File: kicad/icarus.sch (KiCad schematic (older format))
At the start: 80 parts, among them J1 CAN Bus, J2 CAN Bus, J3 SWD Programming, J4 USB_B_Micro, U1 MAX15062A, U10 XT30, U11 XT30, U12 XT30, U13 LT1787HVIMS8PBF, U14 USBLC6-2SC6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

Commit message: Updated BOM, updated layout to fix design rules
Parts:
- CR1, CR2: symbol SMBJ51CA-E3&slash_52:SMBJ51CA-E3_52 -> icarus-rescue:SMBJ51CA-E3_52-SMBJ51CA-E3&slash_52
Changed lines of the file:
@@
 	7200 3525 7475 3525
 $Comp
-L SMBJ51CA-E3&slash_52:SMBJ51CA-E3_52 CR1
+L icarus-rescue:SMBJ51CA-E3_52-SMBJ51CA-E3&slash_52 CR1
 U 1 1 608E4AFE
 P 7475 3925
@@
 Connection ~ 7475 3525
 $Comp
-L SMBJ51CA-E3&slash_52:SMBJ51CA-E3_52 CR2
+L icarus-rescue:SMBJ51CA-E3_52-SMBJ51CA-E3&slash_52 CR2
 U 1 1 608F0D36
 P 7675 3925

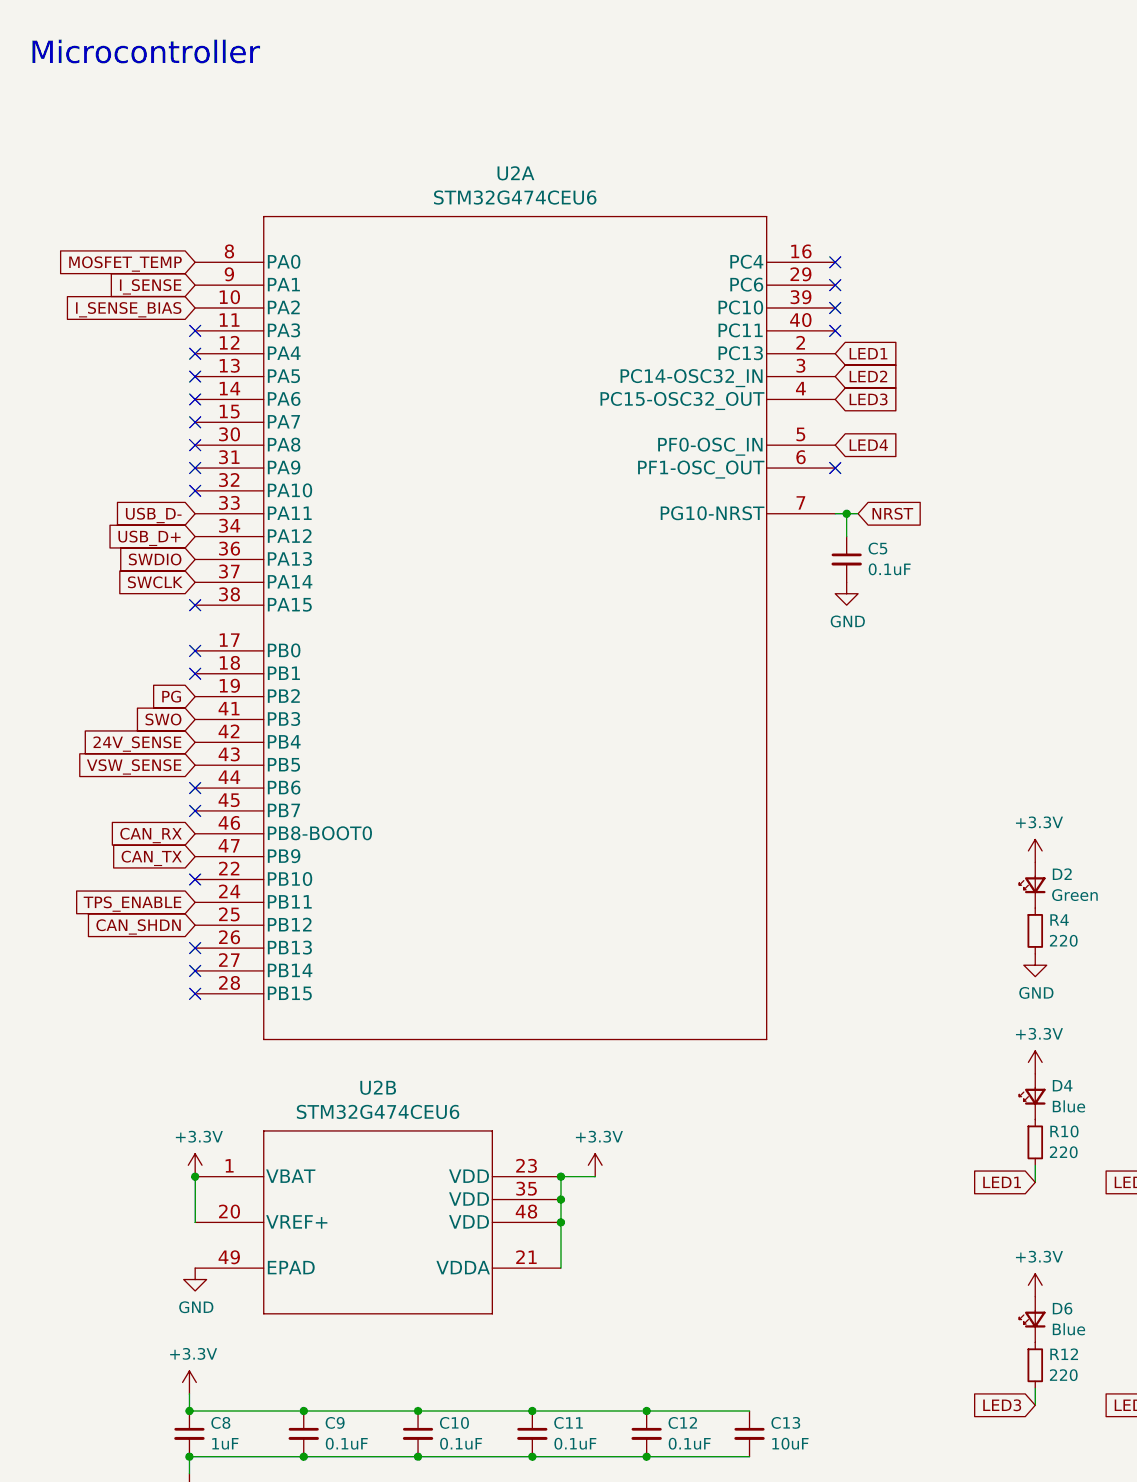
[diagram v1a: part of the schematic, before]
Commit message: Changed MCU due to sourcing problems
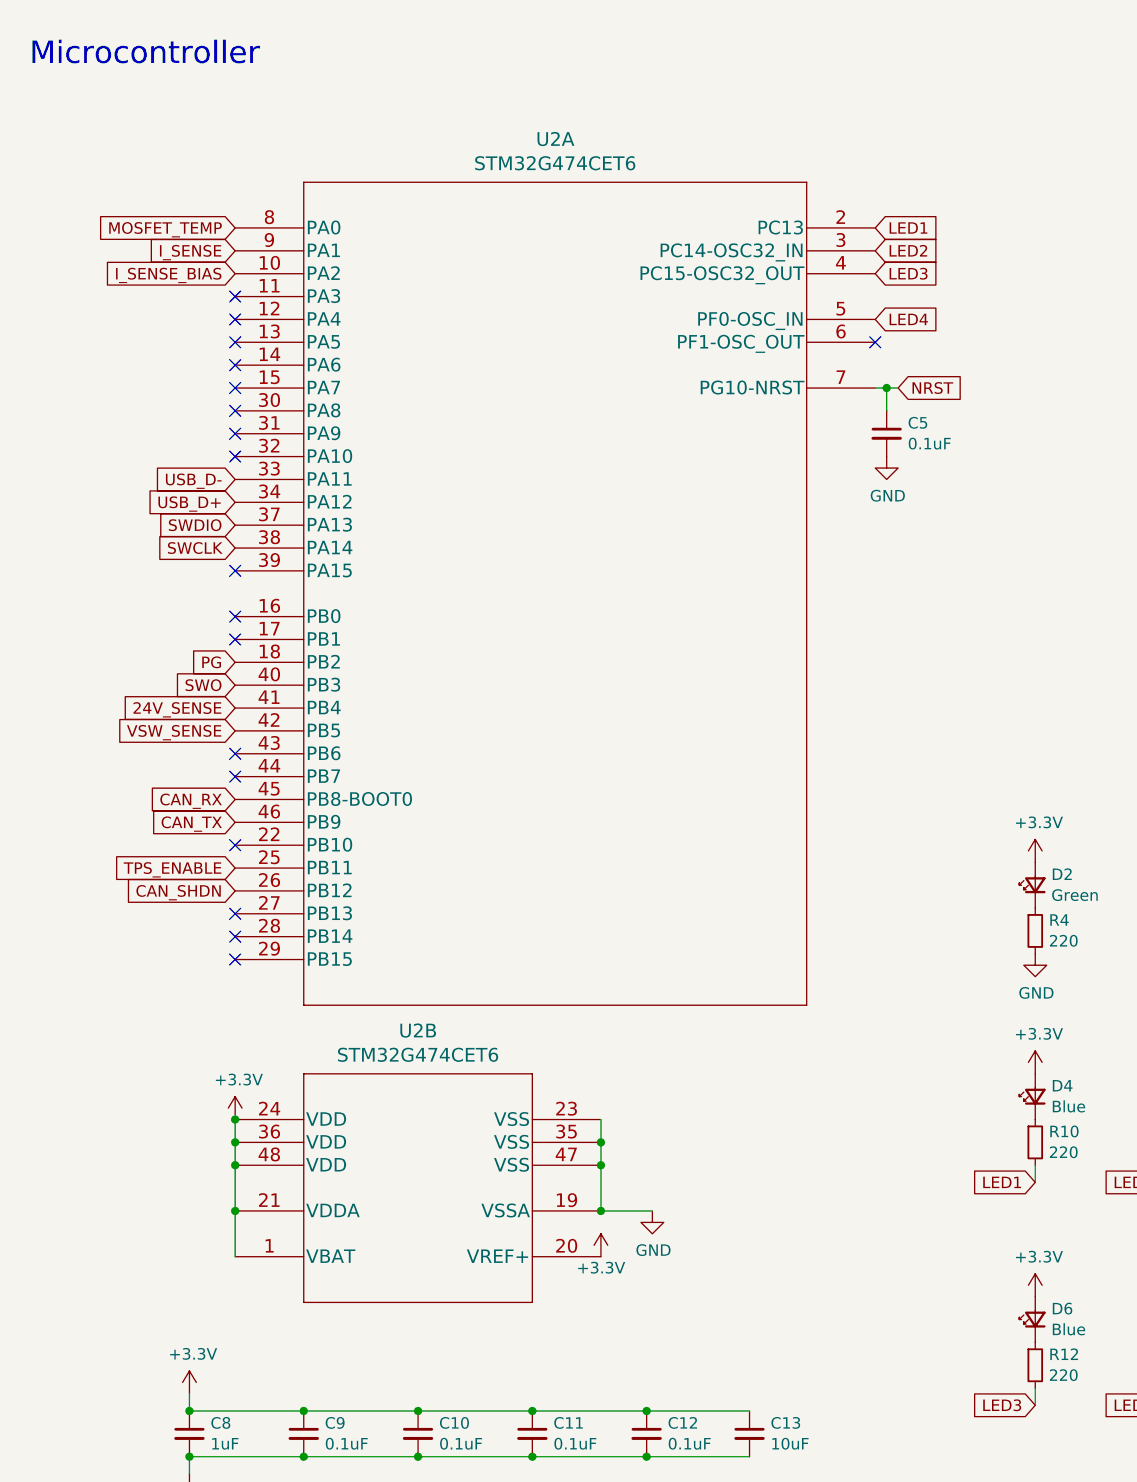
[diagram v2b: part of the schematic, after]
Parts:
- removed U2: STM32G474CEU6, icarus_kicad_lib:STM32G474CEU6, symbol STM32G474CEU6:STM32G474CEU6
- added U2: STM32G474CET6, icarus_kicad_lib:STM32G474CET6, symbol STM32G474CET6:STM32G474CET6
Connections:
- net +3V3: now also U2.1 (VBAT), U2.20 (VREF+), U2.21 (VDDA), U2.24 (VDD), U2.36 (VDD), U2.48 (VDD)
- net 24V_SENSE: now also U2.41 (PB4)
- net CAN_RX: now also U2.45 (PB8-BOOT0)
- net CAN_SHDN: now also U2.26 (PB12)
- net CAN_TX: now also U2.46 (PB9)
- net GND: now also U2.19 (VSSA), U2.23 (VSS), U2.35 (VSS), U2.47 (VSS)
- net I_SENSE: now also U2.9 (PA1)
- net I_SENSE_BIAS: now also U2.10 (PA2)
- net LED1: now also U2.2 (PC13)
- net LED2: now also U2.3 (PC14-OSC32_IN)
- net LED3: now also U2.4 (PC15-OSC32_OUT)
- net LED4: now also U2.5 (PF0-OSC_IN)
- net MOSFET_TEMP: now also U2.8 (PA0)
- net NRST: now also U2.7 (PG10-NRST)
- net PG: now also U2.18 (PB2)
- net SWCLK: now also U2.38 (PA14)
- net SWDIO: now also U2.37 (PA13)
- net SWO: now also U2.40 (PB3)
- net TPS_ENABLE: now also U2.25 (PB11)
- net USB_D+: now also U2.34 (PA12)
- net USB_D-: now also U2.33 (PA11)
- net VSW_SENSE: now also U2.42 (PB5)
- no-connect marks 28 -> 24
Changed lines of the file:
@@
 $EndDescr
-$Comp
-L STM32G474CEU6:STM32G474CEU6 U2
-U 2 1 6042C706
-P 1250 5525
-F 0 "U2" H 2050 5912 60  0000 C CNN
-F 1 "STM32G474CEU6" H 2050 5806 60  0000 C CNN
-F 2 "icarus_kicad_lib:STM32G474CEU6" H 2650 5765 60  0001 C CNN
-F 3 "" H 1250 5525 60  0000 C CNN
-	2    1250 5525
-	1    0    0    -1
-$EndComp
 $Comp
 L power:+3.3V #PWR039
@@
 $EndComp
 $Comp
-L power:GND #PWR035
-U 1 1 6043271D
-P 1250 5925
-F 0 "#PWR035" H 1250 5675 50  0001 C CNN
-F 1 "GND" H 1255 5752 50  0000 C CNN
-F 2 "" H 1250 5925 50  0001 C CNN
-F 3 "" H 1250 5925 50  0001 C CNN
-	1    1250 5925
-	1    0    0    -1
-$EndComp
-$Comp
 L Device:C_Small C8
 U 1 1 60432DFD
@@
 	1225 6750 1225 6825
 Connection ~ 1225 6750
-$Comp
-L power:+3.3V #PWR032
-U 1 1 6043BA2D
-P 3000 5525
-F 0 "#PWR032" H 3000 5375 50  0001 C CNN
-F 1 "+3.3V" H 3015 5698 50  0000 C CNN
-F 2 "" H 3000 5525 50  0001 C CNN
-F 3 "" H 3000 5525 50  0001 C CNN
-	1    3000 5525
-	1    0    0    -1
-$EndComp
-Wire Wire Line
-	2850 5925 2850 5725
-Connection ~ 2850 5625
-Wire Wire Line
-	2850 5625 2850 5525
-Connection ~ 2850 5725
-Wire Wire Line
-	2850 5725 2850 5625
-Wire Wire Line
-	2850 5525 3000 5525
-Connection ~ 2850 5525
-$Comp
-L power:+3.3V #PWR031
-U 1 1 6043DD57
-P 1250 5525
-F 0 "#PWR031" H 1250 5375 50  0001 C CNN
-F 1 "+3.3V" H 1265 5698 50  0000 C CNN
-F 2 "" H 1250 5525 50  0001 C CNN
-F 3 "" H 1250 5525 50  0001 C CNN
-	1    1250 5525
-	1    0    0    -1
-$EndComp
 $Comp
 L Interface_CAN_LIN:TCAN334G U3
@@
 Text GLabel 10150 6175 2    50   Input ~ 0
 PG
-Text GLabel 1250 3525 0    50   Input ~ 0
-SWO
-Text GLabel 1250 2925 0    50   Input ~ 0
-SWCLK
-Text GLabel 1250 2825 0    50   Input ~ 0
-SWDIO
-Text GLabel 1250 4025 0    50   Input ~ 0
-CAN_RX
-Text GLabel 1250 4125 0    50   Input ~ 0
-CAN_TX
-Text GLabel 1250 2625 0    50   Input ~ 0
-USB_D-
-Text GLabel 1250 2725 0    50   Input ~ 0
-USB_D+
-Text GLabel 4150 2625 2    50   Input ~ 0
-NRST
 Text GLabel 8750 6375 0    50   Input ~ 0
 VSENSE_LOW
@@
 LED1
 $Comp
-L STM32G474CEU6:STM32G474CEU6 U2
-U 1 1 6042A58C
-P 1250 1525
-F 0 "U2" H 2650 1912 60  0000 C CNN
-F 1 "STM32G474CEU6" H 2650 1806 60  0000 C CNN
-F 2 "icarus_kicad_lib:STM32G474CEU6" H 2650 1765 60  0001 C CNN
-F 3 "" H 1250 1525 60  0000 C CNN
-	1    1250 1525
-	1    0    0    -1
-$EndComp
-$Comp
 L power:+3.3V #PWR020
 U 1 1 607D3F90
@@
 LED2
 $Comp
-L Device:C_Small C5
-U 1 1 607ECFE5
-P 4100 2825
-F 0 "C5" H 4192 2871 50  0000 L CNN
-F 1 "0.1uF" H 4192 2780 50  0000 L CNN
-F 2 "Capacitor_SMD:C_0402_1005Metric" H 4100 2825 50  0001 C CNN
-F 3 "~" H 4100 2825 50  0001 C CNN
-	1    4100 2825
-	1    0    0    -1
-$EndComp
-Wire Wire Line
-	4150 2625 4100 2625
-Wire Wire Line
-	4100 2725 4100 2625
-Connection ~ 4100 2625
-Wire Wire Line
-	4100 2625 4050 2625
-$Comp
-L power:GND #PWR012
-U 1 1 6081256A
-P 4100 2925
-F 0 "#PWR012" H 4100 2675 50  0001 C CNN
-F 1 "GND" H 4105 2752 50  0000 C CNN
-F 2 "" H 4100 2925 50  0001 C CNN
-F 3 "" H 4100 2925 50  0001 C CNN
-	1    4100 2925
-	1    0    0    -1
-$EndComp
-Wire Wire Line
-	1250 5725 1250 5525
-Connection ~ 1250 5525
-$Comp
 L lt1787hvims8pbf:LT1787HVIMS8PBF U13
 U 1 1 608530FA
@@
 Text GLabel 6675 9825 0    50   Input ~ 0
 MOSFET_TEMP
-Text GLabel 1250 1525 0    50   Input ~ 0
-MOSFET_TEMP
-Text GLabel 1250 1725 0    50   Input ~ 0
-I_SENSE_BIAS
-Text GLabel 1250 4425 0    50   Input ~ 0
-CAN_SHDN
 $Comp
 L power:GND #PWR06
@@
 Wire Wire Line
 	8175 3525 8350 3525
-Text GLabel 4050 1925 2    50   Input ~ 0
-LED1
-Text GLabel 4050 2025 2    50   Input ~ 0
-LED2
-Text GLabel 1250 4325 0    50   Input ~ 0
-TPS_ENABLE
 $Comp
 L Device:C_Small C13
@@
 Text GLabel 5500 6525 0    50   Input ~ 0
 LED4
-Text GLabel 4050 2125 2    50   Input ~ 0
-LED3
-Text GLabel 4050 2325 2    50   Input ~ 0
-LED4
 Wire Wire Line
 	4925 6450 4925 6525
@@
 	1    0    0    -1
 $EndComp
-Text GLabel 1250 1625 0    50   Input ~ 0
-I_SENSE
-Text GLabel 1250 3625 0    50   Input ~ 0
-24V_SENSE
-Text GLabel 1250 3725 0    50   Input ~ 0
-VSW_SENSE
 Text Notes 15425 5400 0    50   ~ 0
 XT30s
@@
 Wire Wire Line
 	10025 4450 10150 4450
-NoConn ~ 1250 1925
-NoConn ~ 1250 2125
-NoConn ~ 1250 2325
-NoConn ~ 1250 2425
-NoConn ~ 1250 2525
-NoConn ~ 1250 3025
-NoConn ~ 1250 4225
-NoConn ~ 1250 4525
-NoConn ~ 1250 4625
-NoConn ~ 1250 4725
-NoConn ~ 4050 2425
-NoConn ~ 4050 1825
-NoConn ~ 4050 1725
-NoConn ~ 4050 1625
-NoConn ~ 4050 1525
 $Comp
 L icarus-rescue:PSMN4R8-100BSEJ-psmn4r8-100bsej MOSFET1
@@
 	1    0    0    -1
 $EndComp
-NoConn ~ 1250 3325
-NoConn ~ 1250 3925
-NoConn ~ 1250 1825
-NoConn ~ 1250 2225
-NoConn ~ 1250 2025
-NoConn ~ 1250 3225
 Wire Wire Line
 	9650 3525 11125 3525
@@
 	1    0    0    -1
 $EndComp
-Text GLabel 1250 3425 0    50   Input ~ 0
-PG
 $Comp
 L Device:R_Small R17
@@
 	10025 8950 9525 8950
 Connection ~ 9525 8950
-NoConn ~ 1250 3825
 $Comp
 L power:GNDPWR #PWR0101
@@
 NoConn ~ 13175 6425
 NoConn ~ 13175 6625
+$Comp
+L STM32G474CET6:STM32G474CET6 U2
+U 1 1 605EDEF6
+P 1425 1375
+F 0 "U2" H 2825 1762 60  0000 C CNN
+F 1 "STM32G474CET6" H 2825 1656 60  0000 C CNN
+F 2 "icarus_kicad_lib:STM32G474CET6" H 2825 1615 60  0001 C CNN
+F 3 "" H 1425 1375 60  0000 C CNN
+	1    1425 1375
+	1    0    0    -1
+$EndComp
+$Comp
+L STM32G474CET6:STM32G474CET6 U2
+U 2 1 605F9058
+P 1425 5275
+F 0 "U2" H 2225 5662 60  0000 C CNN
+F 1 "STM32G474CET6" H 2225 5556 60  0000 C CNN
+F 2 "icarus_kicad_lib:STM32G474CET6" H 2825 5515 60  0001 C CNN
+F 3 "" H 1425 5275 60  0000 C CNN
+	2    1425 5275
+	1    0    0    -1
+$EndComp
+$Comp
+L power:+3.3V #PWR0107
+U 1 1 6060CB55
+P 1425 5275
+F 0 "#PWR0107" H 1425 5125 50  0001 C CNN
+F 1 "+3.3V" H 1440 5448 50  0000 C CNN
+F 2 "" H 1425 5275 50  0001 C CNN
+F 3 "" H 1425 5275 50  0001 C CNN
+	1    1425 5275
+	1    0    0    -1
+$EndComp
+Wire Wire Line
+	1425 5275 1425 5375
+Connection ~ 1425 5275
+Connection ~ 1425 5375
+Wire Wire Line
+	1425 5375 1425 5475
+Connection ~ 1425 5475
+Wire Wire Line
+	1425 5475 1425 5675
+Connection ~ 1425 5675
+Wire Wire Line
+	1425 5675 1425 5875
+$Comp
+L power:+3.3V #PWR0108
+U 1 1 6061CA59
+P 3025 5875
+F 0 "#PWR0108" H 3025 5725 50  0001 C CNN
+F 1 "+3.3V" H 3025 5825 50  0000 C CNN
+F 2 "" H 3025 5875 50  0001 C CNN
+F 3 "" H 3025 5875 50  0001 C CNN
+	1    3025 5875
+	1    0    0    -1
+$EndComp
+$Comp
+L power:GND #PWR0109
+U 1 1 6061F17E
+P 3250 5675
+F 0 "#PWR0109" H 3250 5425 50  0001 C CNN
+F 1 "GND" H 3255 5502 50  0000 C CNN
+F 2 "" H 3250 5675 50  0001 C CNN
+F 3 "" H 3250 5675 50  0001 C CNN
+	1    3250 5675
+	1    0    0    -1
+$EndComp
+Wire Wire Line
+	3250 5675 3025 5675
+Wire Wire Line
+	3025 5675 3025 5475
+Connection ~ 3025 5675
+Connection ~ 3025 5375
+Wire Wire Line
+	3025 5375 3025 5275
+Connection ~ 3025 5475
+Wire Wire Line
+	3025 5475 3025 5375
+Text GLabel 1425 1375 0    50   Input ~ 0
+MOSFET_TEMP
+Text GLabel 1425 1475 0    50   Input ~ 0
+I_SENSE
+Text GLabel 1425 1575 0    50   Input ~ 0
+I_SENSE_BIAS
+Text GLabel 1425 2475 0    50   Input ~ 0
+USB_D-
+Text GLabel 1425 2575 0    50   Input ~ 0
+USB_D+
+Text GLabel 1425 3375 0    50   Input ~ 0
+SWO
+Text GLabel 1425 2775 0    50   Input ~ 0
+SWCLK
+Text GLabel 1425 2675 0    50   Input ~ 0
+SWDIO
+Text GLabel 1425 3875 0    50   Input ~ 0
+CAN_RX
+Text GLabel 1425 3975 0    50   Input ~ 0
+CAN_TX
+Text GLabel 1425 4275 0    50   Input ~ 0
+CAN_SHDN
+Text GLabel 1425 4175 0    50   Input ~ 0
+TPS_ENABLE
+Text GLabel 1425 3475 0    50   Input ~ 0
+24V_SENSE
+Text GLabel 1425 3575 0    50   Input ~ 0
+VSW_SENSE
+Text GLabel 1425 3275 0    50   Input ~ 0
+PG
+Text GLabel 4225 1375 2    50   Input ~ 0
+LED1
+Text GLabel 4225 1475 2    50   Input ~ 0
+LED2
+Text GLabel 4225 1575 2    50   Input ~ 0
+LED3
+Text GLabel 4225 1775 2    50   Input ~ 0
+LED4
+Text GLabel 4325 2075 2    50   Input ~ 0
+NRST
+$Comp
+L Device:C_Small C5
+U 1 1 60685E2A
+P 4275 2275
+F 0 "C5" H 4367 2321 50  0000 L CNN
+F 1 "0.1uF" H 4367 2230 50  0000 L CNN
+F 2 "Capacitor_SMD:C_0402_1005Metric" H 4275 2275 50  0001 C CNN
+F 3 "~" H 4275 2275 50  0001 C CNN
+	1    4275 2275
+	1    0    0    -1
+$EndComp
+Wire Wire Line
+	4325 2075 4275 2075
+Wire Wire Line
+	4275 2175 4275 2075
+Connection ~ 4275 2075
+Wire Wire Line
+	4275 2075 4225 2075
+$Comp
+L power:GND #PWR0110
+U 1 1 60685E34
+P 4275 2375
+F 0 "#PWR0110" H 4275 2125 50  0001 C CNN
+F 1 "GND" H 4280 2202 50  0000 C CNN
+F 2 "" H 4275 2375 50  0001 C CNN
+F 3 "" H 4275 2375 50  0001 C CNN
+	1    4275 2375
+	1    0    0    -1
+$EndComp
+NoConn ~ 1425 1675
+NoConn ~ 1425 1775
+NoConn ~ 1425 1875
+NoConn ~ 1425 1975
+NoConn ~ 1425 2075
+NoConn ~ 1425 2175
+NoConn ~ 1425 2275
+NoConn ~ 1425 2375
+NoConn ~ 1425 2875
+NoConn ~ 1425 3075
+NoConn ~ 1425 3175
+NoConn ~ 1425 3675
+NoConn ~ 1425 3775
+NoConn ~ 1425 4075
+NoConn ~ 1425 4375
+NoConn ~ 1425 4475
+NoConn ~ 1425 4575
+NoConn ~ 4225 1875
 $EndSCHEMATC
